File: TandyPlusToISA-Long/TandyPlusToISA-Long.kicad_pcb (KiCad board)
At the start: 2 copper layers, 83.6 x 17.7 mm, 2 parts, among them J1 Bus_ISA_8bit, J3 TANDY PLUS HEADER

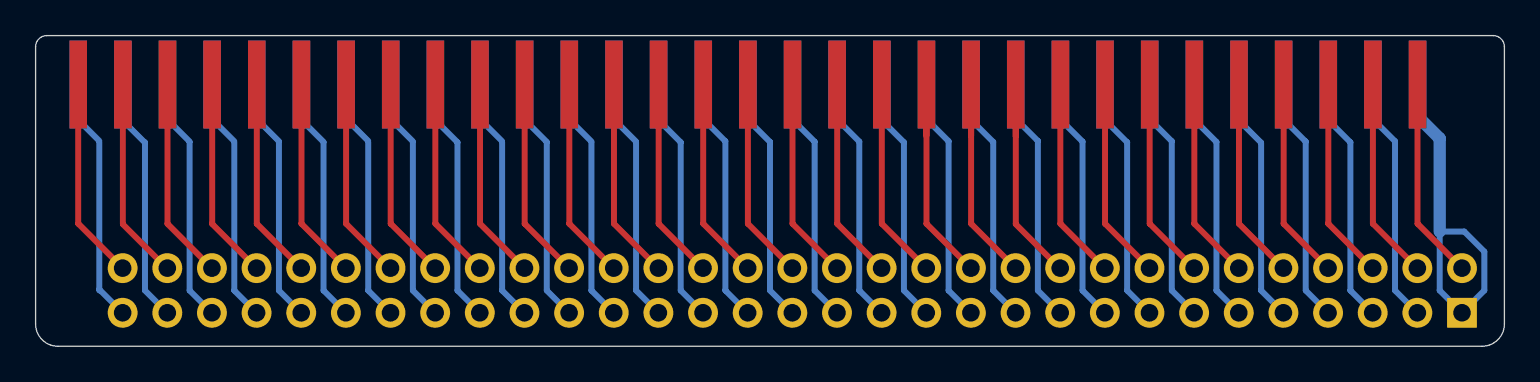
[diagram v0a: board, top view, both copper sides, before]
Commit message: Shifted Plus to ISA adapters a little, updated tested status
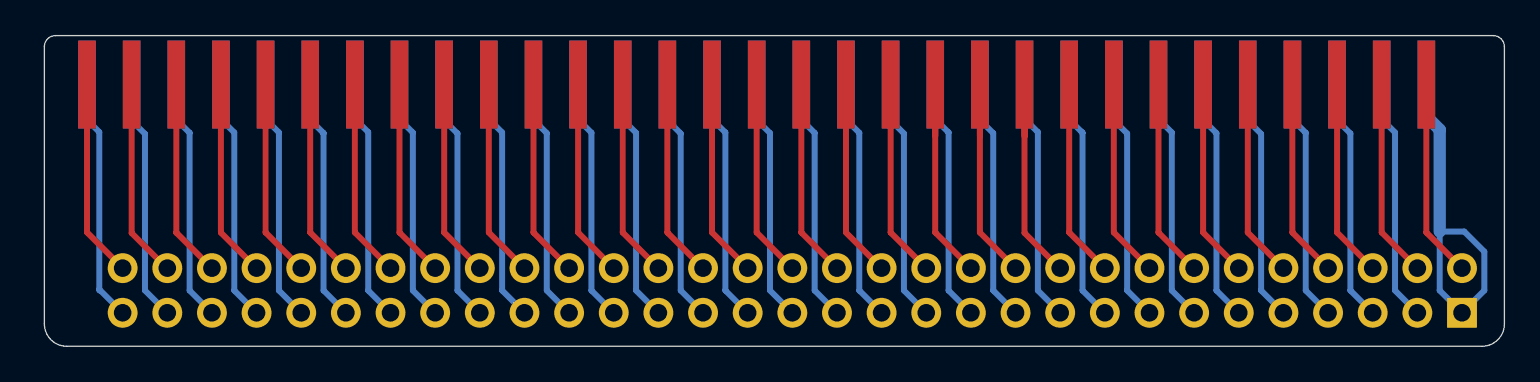
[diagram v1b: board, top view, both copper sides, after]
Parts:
- moved J1 0.50 mm to (173.2, 105.1)
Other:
- board size 83.6 x 17.7 mm -> 83.1 x 17.7 mm
